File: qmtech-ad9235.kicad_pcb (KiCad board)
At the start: 4 copper layers, 56 x 65 mm, 51 parts

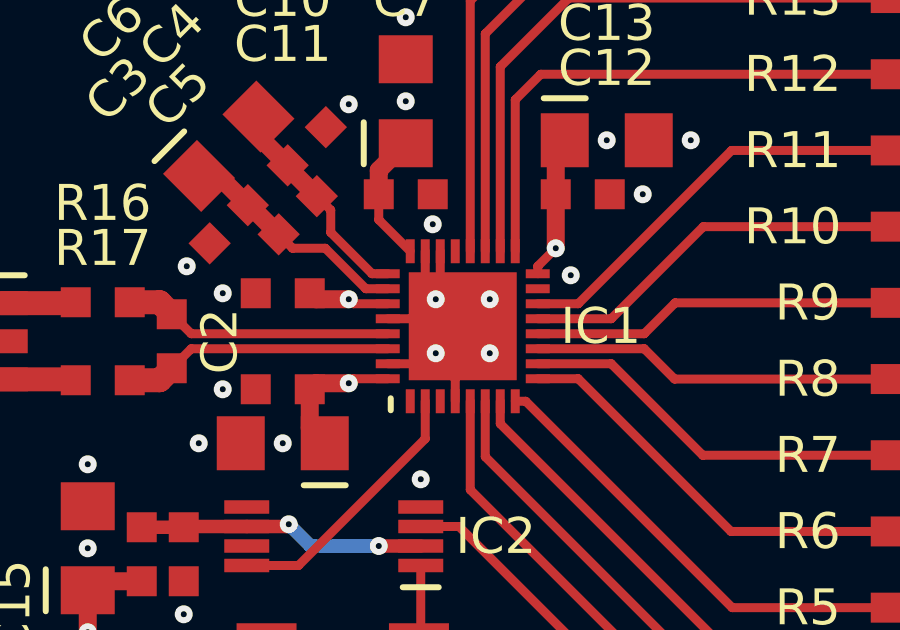
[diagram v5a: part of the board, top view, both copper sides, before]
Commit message: improve LFCSP32
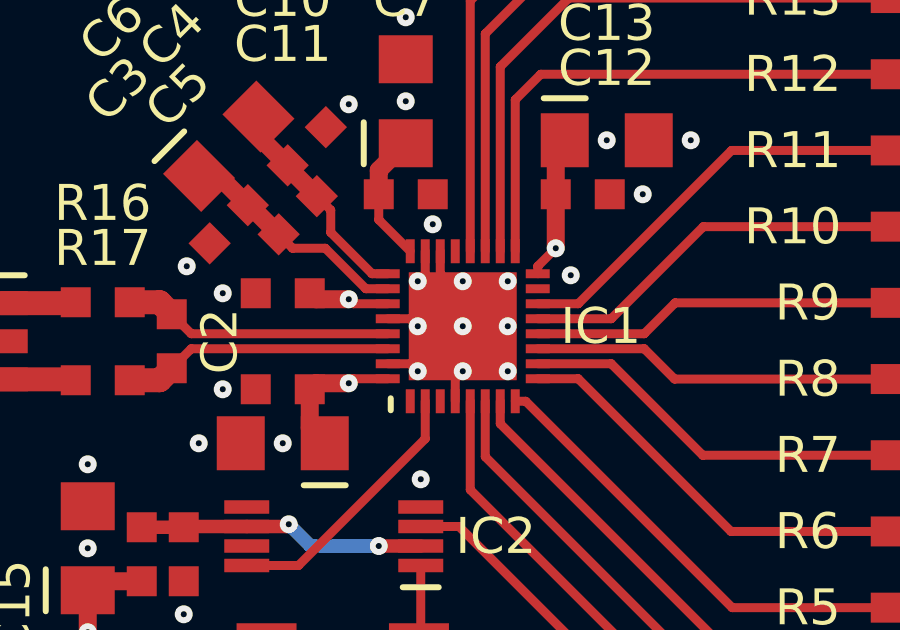
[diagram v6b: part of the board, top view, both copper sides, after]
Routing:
- net GND: track 8.43 -> 6.02 mm, vias 47 -> 52
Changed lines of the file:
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@@
     (fp_line (start -2.8 -2.4) (end -2.4 -2.4)
       (stroke (width 0.2) (type solid)) (layer "F.SilkS"))
+    (pad "" smd rect (at -0.8 -0.8 90) (size 1.2 1.2) (layers "F.Paste"))
+    (pad "" smd rect (at -0.8 0.8 90) (size 1.2 1.2) (layers "F.Paste"))
+    (pad "" smd rect (at 0.8 -0.8 90) (size 1.2 1.2) (layers "F.Paste"))
+    (pad "" smd rect (at 0.8 0.8 90) (size 1.2 1.2) (layers "F.Paste"))
     (pad "1" smd rect (at -2.5 -1.75 90) (size 0.8 0.3) (layers "F.Cu" "F.Paste" "F.Mask"))
     (pad "2" smd rect (at -2.5 -1.25 90) (size 0.8 0.3) (layers "F.Cu" "F.Paste" "F.Mask")
@@
     (pad "32" smd rect (at -1.75 -2.5 180) (size 0.8 0.3) (layers "F.Cu" "F.Paste" "F.Mask")
       (net 15 "AVDD"))
-    (pad "33" smd rect (at 0 0 90) (size 3.6 3.6) (layers "F.Cu" "F.Paste" "F.Mask")
+    (pad "33" smd rect (at 0 0 90) (size 3.6 3.6) (layers "F.Cu" "F.Mask")
       (net 18 "GND"))
   )
@@
   (segment (start 100.75 68.6) (end 100.75 61.35) (width 0.3) (layer "F.Cu") (net 17))
   (segment (start 104.48 57.62) (end 114.1 57.62) (width 0.3) (layer "F.Cu") (net 17))
-  (segment (start 98.75 69.85) (end 99 70.1) (width 0.3) (layer "F.Cu") (net 18))
-  (segment (start 97.5 72.35) (end 98.75 72.35) (width 0.3) (layer "F.Cu") (net 18))
-  (segment (start 99.75 72.85) (end 99 72.1) (width 0.3) (layer "F.Cu") (net 18))
+  (segment (start 98.25 72.35) (end 98.5 72.6) (width 0.3) (layer "F.Cu") (net 18))
+  (segment (start 99.25 69.35) (end 99.5 69.6) (width 0.3) (layer "F.Cu") (net 18))
   (segment (start 99.75 73.6) (end 99.75 72.85) (width 0.3) (layer "F.Cu") (net 18))
-  (segment (start 98.75 68.6) (end 98.75 69.85) (width 0.3) (layer "F.Cu") (net 18))
-  (segment (start 98.25 70.85) (end 99 70.1) (width 0.3) (layer "F.Cu") (net 18))
-  (segment (start 98.75 72.35) (end 99 72.1) (width 0.3) (layer "F.Cu") (net 18))
+  (segment (start 98.75 68.6) (end 98.75 69.35) (width 0.3) (layer "F.Cu") (net 18))
+  (segment (start 99.5 69.6) (end 100 69.6) (width 0.3) (layer "F.Cu") (net 18))
+  (segment (start 99.25 68.6) (end 99.25 69.35) (width 0.3) (layer "F.Cu") (net 18))
   (segment (start 97.5 70.85) (end 98.25 70.85) (width 0.3) (layer "F.Cu") (net 18))
-  (segment (start 99.25 69.85) (end 99 70.1) (width 0.3) (layer "F.Cu") (net 18))
-  (segment (start 99.25 68.6) (end 99.25 69.85) (width 0.3) (layer "F.Cu") (net 18))
+  (segment (start 99.75 72.85) (end 100 72.6) (width 0.3) (layer "F.Cu") (net 18))
+  (segment (start 98.75 69.35) (end 98.5 69.6) (width 0.3) (layer "F.Cu") (net 18))
+  (segment (start 97.5 72.35) (end 98.25 72.35) (width 0.3) (layer "F.Cu") (net 18))
+  (segment (start 98.25 70.85) (end 98.5 71.1) (width 0.3) (layer "F.Cu") (net 18))
   (via (at 83.95 91.9) (size 0.6) (drill 0.2) (layers "F.Cu" "B.Cu") (free) (net 18))
   (via (at 96.9 85.7) (size 0.6) (drill 0.2) (layers "F.Cu" "B.Cu") (free) (net 18))
@@
   (via (at 83.9 84.9) (size 0.6) (drill 0.2) (layers "F.Cu" "B.Cu") (free) (net 18))
   (via (at 104 91.9) (size 0.6) (drill 0.2) (layers "F.Cu" "B.Cu") (free) (net 18))
+  (via (at 101.5 71.1) (size 0.6) (drill 0.2) (layers "F.Cu" "B.Cu") (net 18))
   (via (at 83 91.9) (size 0.6) (drill 0.2) (layers "F.Cu" "B.Cu") (free) (net 18))
   (via (at 90.8 69.1) (size 0.6) (drill 0.2) (layers "F.Cu" "B.Cu") (free) (net 18))
-  (via (at 100.9 72) (size 0.6) (drill 0.2) (layers "F.Cu" "B.Cu") (net 18))
+  (via (at 101.5 72.6) (size 0.6) (drill 0.2) (layers "F.Cu" "B.Cu") (net 18))
   (via (at 106 66.7) (size 0.6) (drill 0.2) (layers "F.Cu" "B.Cu") (free) (net 18))
   (via (at 104 88.2) (size 0.6) (drill 0.2) (layers "F.Cu" "B.Cu") (free) (net 18))
   (via (at 81.6 78) (size 0.6) (drill 0.2) (layers "F.Cu" "B.Cu") (free) (net 18))
-  (via (at 100.9 70.2) (size 0.6) (drill 0.2) (layers "F.Cu" "B.Cu") (net 18))
+  (via (at 101.5 69.6) (size 0.6) (drill 0.2) (layers "F.Cu" "B.Cu") (net 18))
   (via (at 104 89.5) (size 0.6) (drill 0.2) (layers "F.Cu" "B.Cu") (free) (net 18))
   (via (at 85 86) (size 0.6) (drill 0.2) (layers "F.Cu" "B.Cu") (free) (net 18))
@@
   (via (at 81.4 71.6) (size 0.6) (drill 0.2) (layers "F.Cu" "B.Cu") (free) (net 18))
   (via (at 90.7 80.7) (size 0.6) (drill 0.2) (layers "F.Cu" "B.Cu") (free) (net 18))
+  (via (at 100 72.6) (size 0.6) (drill 0.2) (layers "F.Cu" "B.Cu") (net 18))
   (via (at 103.6 69.4) (size 0.6) (drill 0.2) (layers "F.Cu" "B.Cu") (free) (net 18))
   (via (at 106 93) (size 0.6) (drill 0.2) (layers "F.Cu" "B.Cu") (free) (net 18))
   (via (at 99 67.7) (size 0.6) (drill 0.2) (layers "F.Cu" "B.Cu") (free) (net 18))
-  (via (at 99.1 72) (size 0.6) (drill 0.2) (layers "F.Cu" "B.Cu") (net 18))
+  (via (at 98.5 72.6) (size 0.6) (drill 0.2) (layers "F.Cu" "B.Cu") (net 18))
   (via (at 104.9 94.1) (size 0.6) (drill 0.2) (layers "F.Cu" "B.Cu") (free) (net 18))
+  (via (at 100 71.1) (size 0.6) (drill 0.2) (layers "F.Cu" "B.Cu") (net 18))
   (via (at 87.5 78.5) (size 0.6) (drill 0.2) (layers "F.Cu" "B.Cu") (free) (net 18))
   (via (at 104.95 91.9) (size 0.6) (drill 0.2) (layers "F.Cu" "B.Cu") (free) (net 18))
@@
   (via (at 83 88.2) (size 0.6) (drill 0.2) (layers "F.Cu" "B.Cu") (free) (net 18))
   (via (at 98.1 60.8) (size 0.6) (drill 0.2) (layers "F.Cu" "B.Cu") (free) (net 18))
+  (via (at 98.5 71.1) (size 0.6) (drill 0.2) (layers "F.Cu" "B.Cu") (net 18))
+  (via (at 100 69.6) (size 0.6) (drill 0.2) (layers "F.Cu" "B.Cu") (net 18))
   (via (at 104.95 87.1) (size 0.6) (drill 0.2) (layers "F.Cu" "B.Cu") (free) (net 18))
-  (via (at 99.1 70.2) (size 0.6) (drill 0.2) (layers "F.Cu" "B.Cu") (net 18))
+  (via (at 98.5 69.6) (size 0.6) (drill 0.2) (layers "F.Cu" "B.Cu") (net 18))
   (via (at 96.2 63.7) (size 0.6) (drill 0.2) (layers "F.Cu" "B.Cu") (free) (net 18))
   (via (at 92 73.2) (size 0.6) (drill 0.2) (layers "F.Cu" "B.Cu") (free) (net 18))

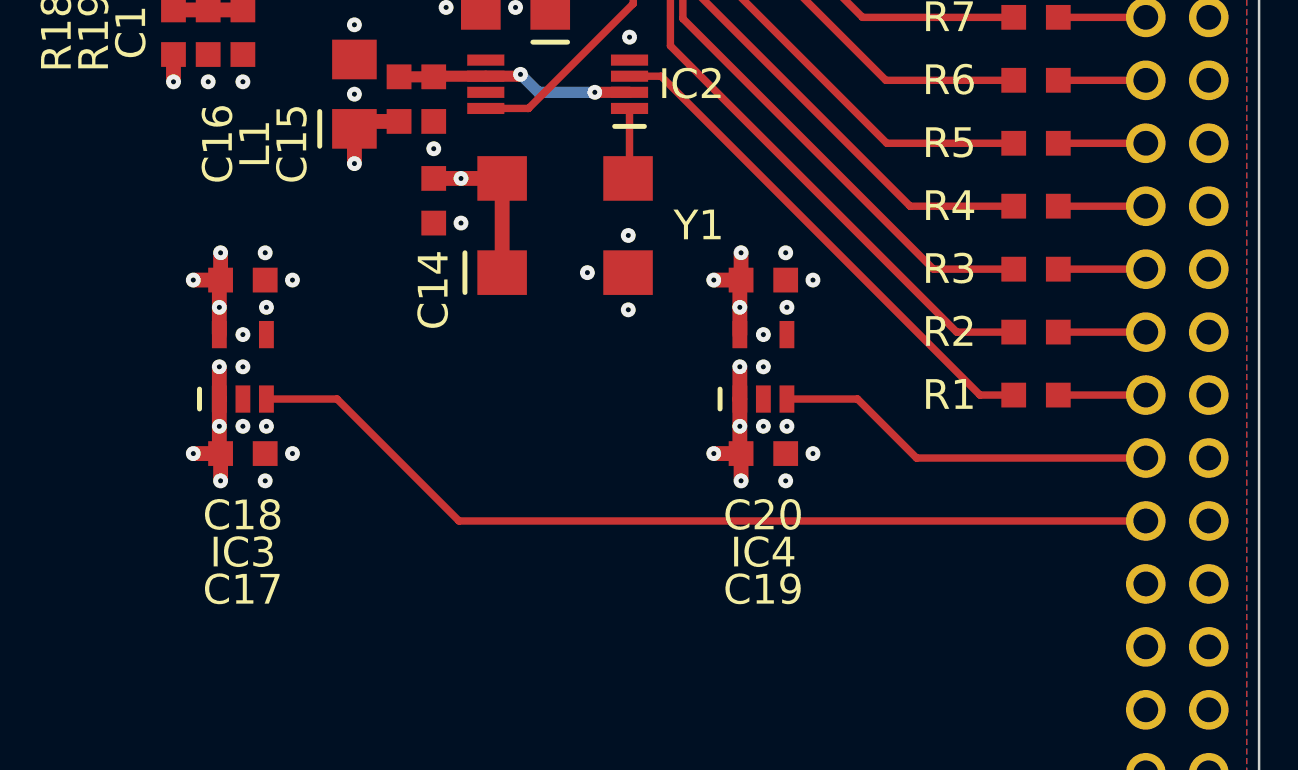
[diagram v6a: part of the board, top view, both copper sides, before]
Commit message: add CVDD regulator
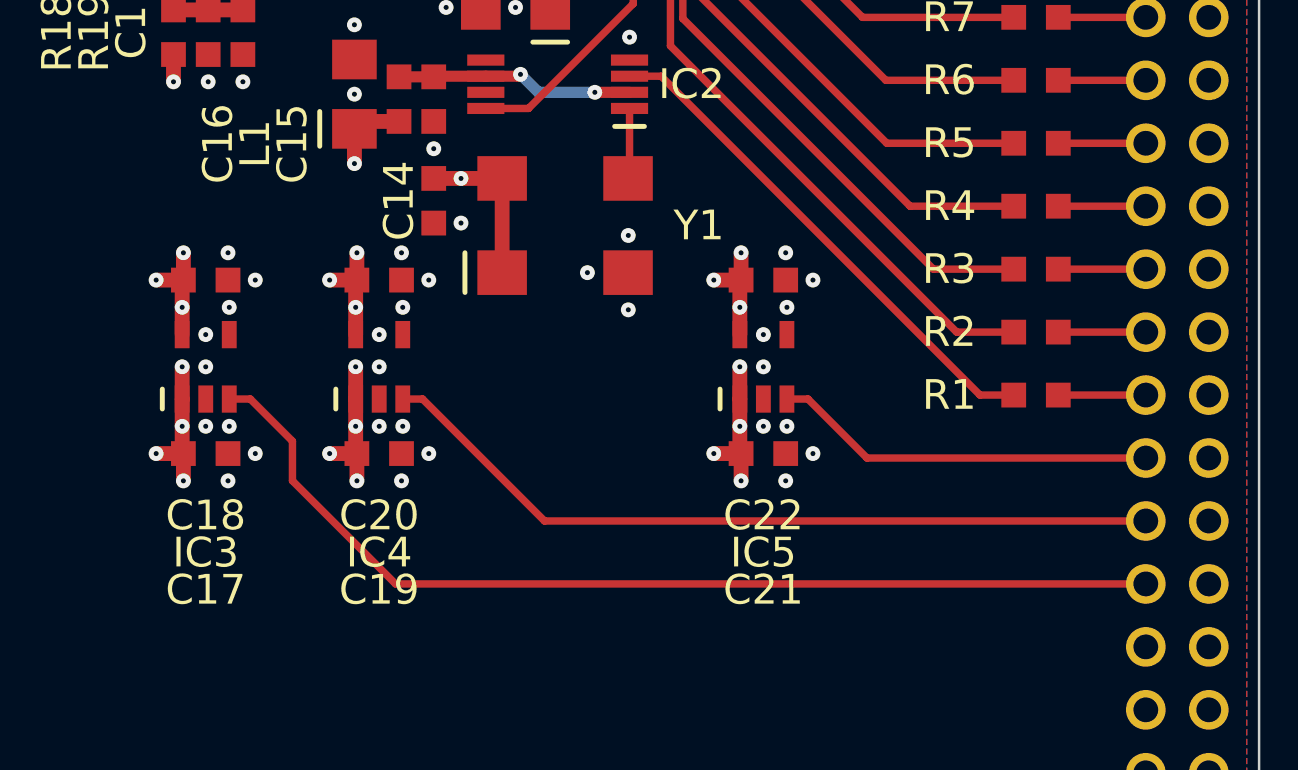
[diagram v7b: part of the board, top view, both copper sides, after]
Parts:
- added C21: , footprints:0603, F.Cu at (104.0, 93.0)
- added C22: , footprints:0603, F.Cu at (104.0, 86.0)
- added IC5: , footprints:SOT23, F.Cu at (104.0, 89.5)
- moved C19 15.5 mm to (88.5, 93.0)
- moved C20 15.5 mm to (88.5, 86.0)
- moved IC4 15.5 mm to (88.5, 89.5)
- moved C17 1.50 mm to (81.5, 93.0)
- moved C18 1.50 mm to (81.5, 86.0)
- moved IC3 1.50 mm to (81.5, 89.5)
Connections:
- C14 pad 1: AVDD -> CVDD
- C16 pad 1: AVDD -> CVDD
- C20 pad 1: DVDD -> CVDD
- CN2 pad 37: AEN -> CEN
- CN2 pad 39: (no net) -> AEN
- IC4 pad 3: DEN -> CEN
- IC4 pad 5: DVDD -> CVDD
- L1 pad 1: AVDD -> CVDD
- Y1 pad 1: AVDD -> CVDD
- Y1 pad 4: AVDD -> CVDD
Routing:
- net CEN: track 0.00 -> 32.0 mm
- net CVDD: track 0.00 -> 14.3 mm, vias 0 -> 5
- net AVDD: track 22.9 -> 13.0 mm, vias 8 -> 6
- net 5V: track 11.4 -> 17.2 mm, vias 8 -> 12
- net AEN: track 37.5 -> 41.0 mm
- net GND: vias 52 -> 61
- added copper zone on In2.Cu, net CVDD
